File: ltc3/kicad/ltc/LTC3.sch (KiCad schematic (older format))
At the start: 0 parts

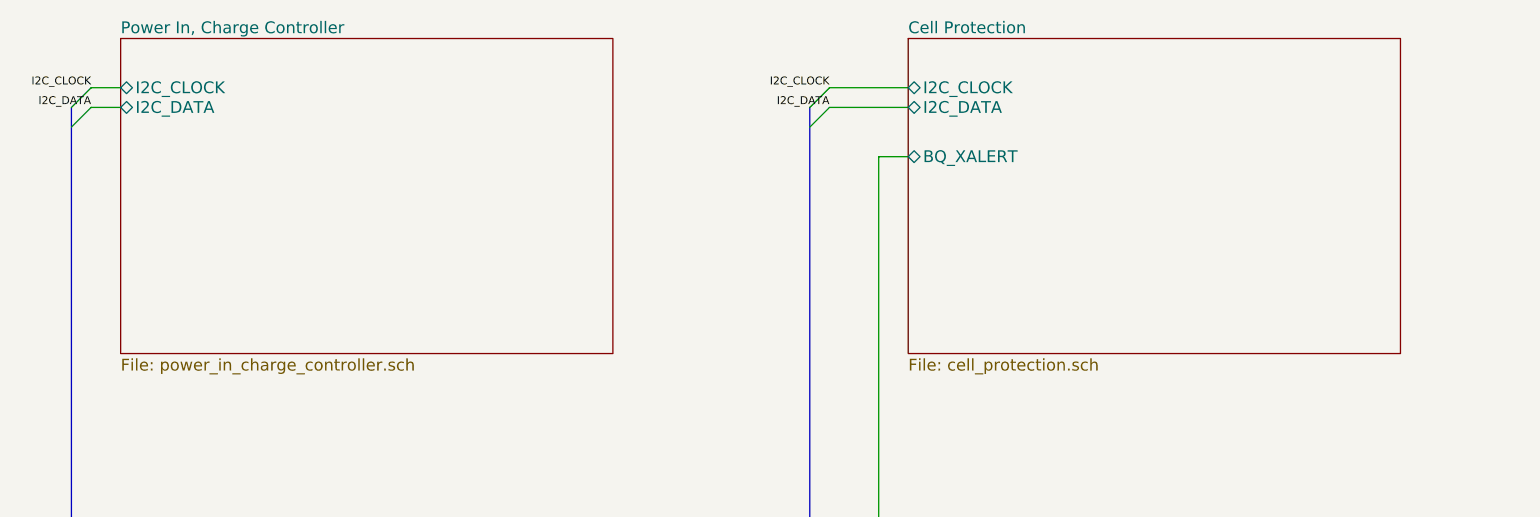
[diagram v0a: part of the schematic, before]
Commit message: LTC3: Split single-board design into two boards.
Separated the charge controller and cell protection circuitry onto its
own board (kicad/charge_controller).  The DC-DC converters,
BeagleBone, external power and triggers, and ignition fire control
circuitry remains together (kicad/ltc).

Both boards have had their schematics updated.  Sub-sheets for
circuitry moved to the other board were removed.  Still more work
remaining, though (e.g., add I2C connectors to Charge Controller
schematic; add battery power connector to LTC board; etc.).

Schematic components were *not* re-annotated to align with new sheet
numbering, as it would screw up the existing layout work (i.e., placed
components would disappear), and that would make us sad engineers.

Both boards have had their PCB layouts converted to four-layer.
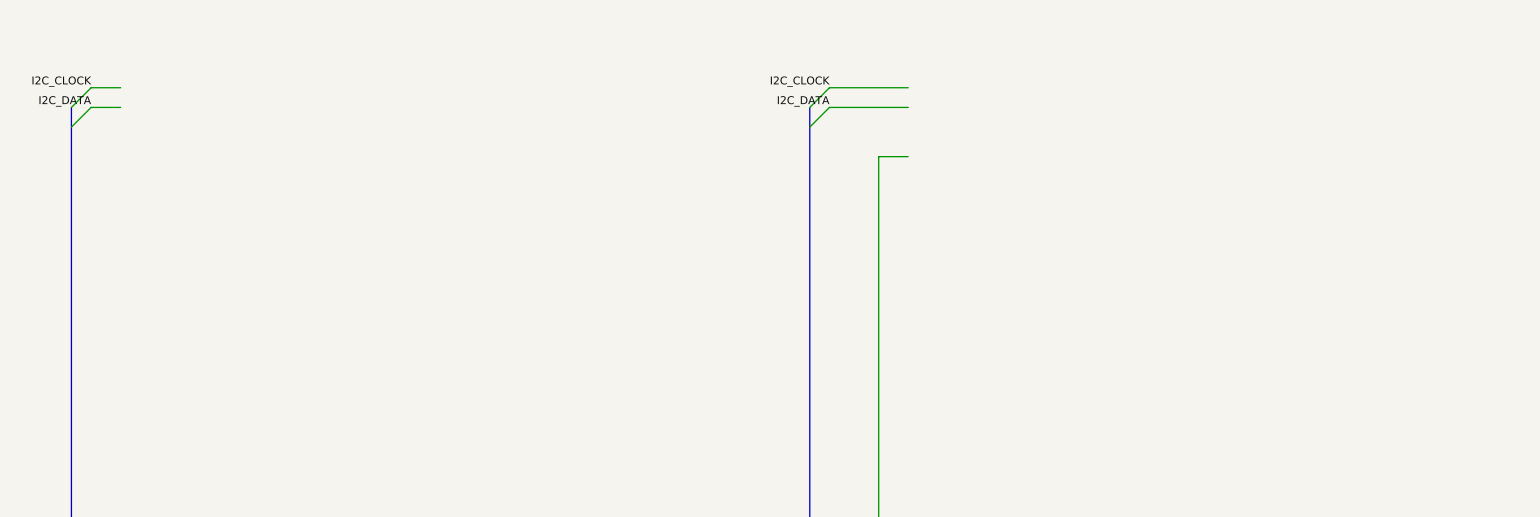
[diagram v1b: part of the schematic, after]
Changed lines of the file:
@@
 LIBS:atmel
 LIBS:audio
-LIBS:bbd
 LIBS:brooktre
 LIBS:cmos4000
@@
 LIBS:transistors
 LIBS:ttl_ieee
-LIBS:Launch_Tower_Computer_III-cache
 EELAYER 25 0
 EELAYER END
 $Descr B 17000 11000
 encoding utf-8
-Sheet 1 8
+Sheet 1 6
 Title "Launch Tower Computer 3 (LTC3)"
 Date "2016-05-09"
@@
 EXT_TRG_EN_4
 $Sheet
-S 1400 1500 2500 1600
-U 56238165
-F0 "Power In, Charge Controller" 60
-F1 "power_in_charge_controller.sch" 60
-F2 "I2C_CLOCK" B L 1400 1750 60
-F3 "I2C_DATA" B L 1400 1850 60
-$EndSheet
-$Sheet
-S 5400 1500 2500 1600
-U 562DD32F
-F0 "Cell Protection" 60
-F1 "cell_protection.sch" 60
-F2 "BQ_XALERT" B L 5400 2100 60
-F3 "I2C_DATA" B L 5400 1850 60
-F4 "I2C_CLOCK" B L 5400 1750 60
-$EndSheet
-$Sheet
 S 5400 6600 2500 1600

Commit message: LTC3: Updates to LTC schematic.
1. Cleaned up top-level sheet.
2. Added board-to-board connectors for power, I2C.
3. Miscelleneous component part selection/changes.
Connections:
- wire segments 38 -> 32
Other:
- note added: "TODO: make use of BQ_XALERT?"
